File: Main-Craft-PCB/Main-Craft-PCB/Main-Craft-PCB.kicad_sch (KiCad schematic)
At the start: 88 parts, among them J1 Conn_01x10, Q23 BC817, Q25 IRFR9014PBF, Q31 BC817, U10 ZLDO1117G50TA, U2 NUCLEO144-F429ZI, U5 74HC14, U9 ZSR330GTA

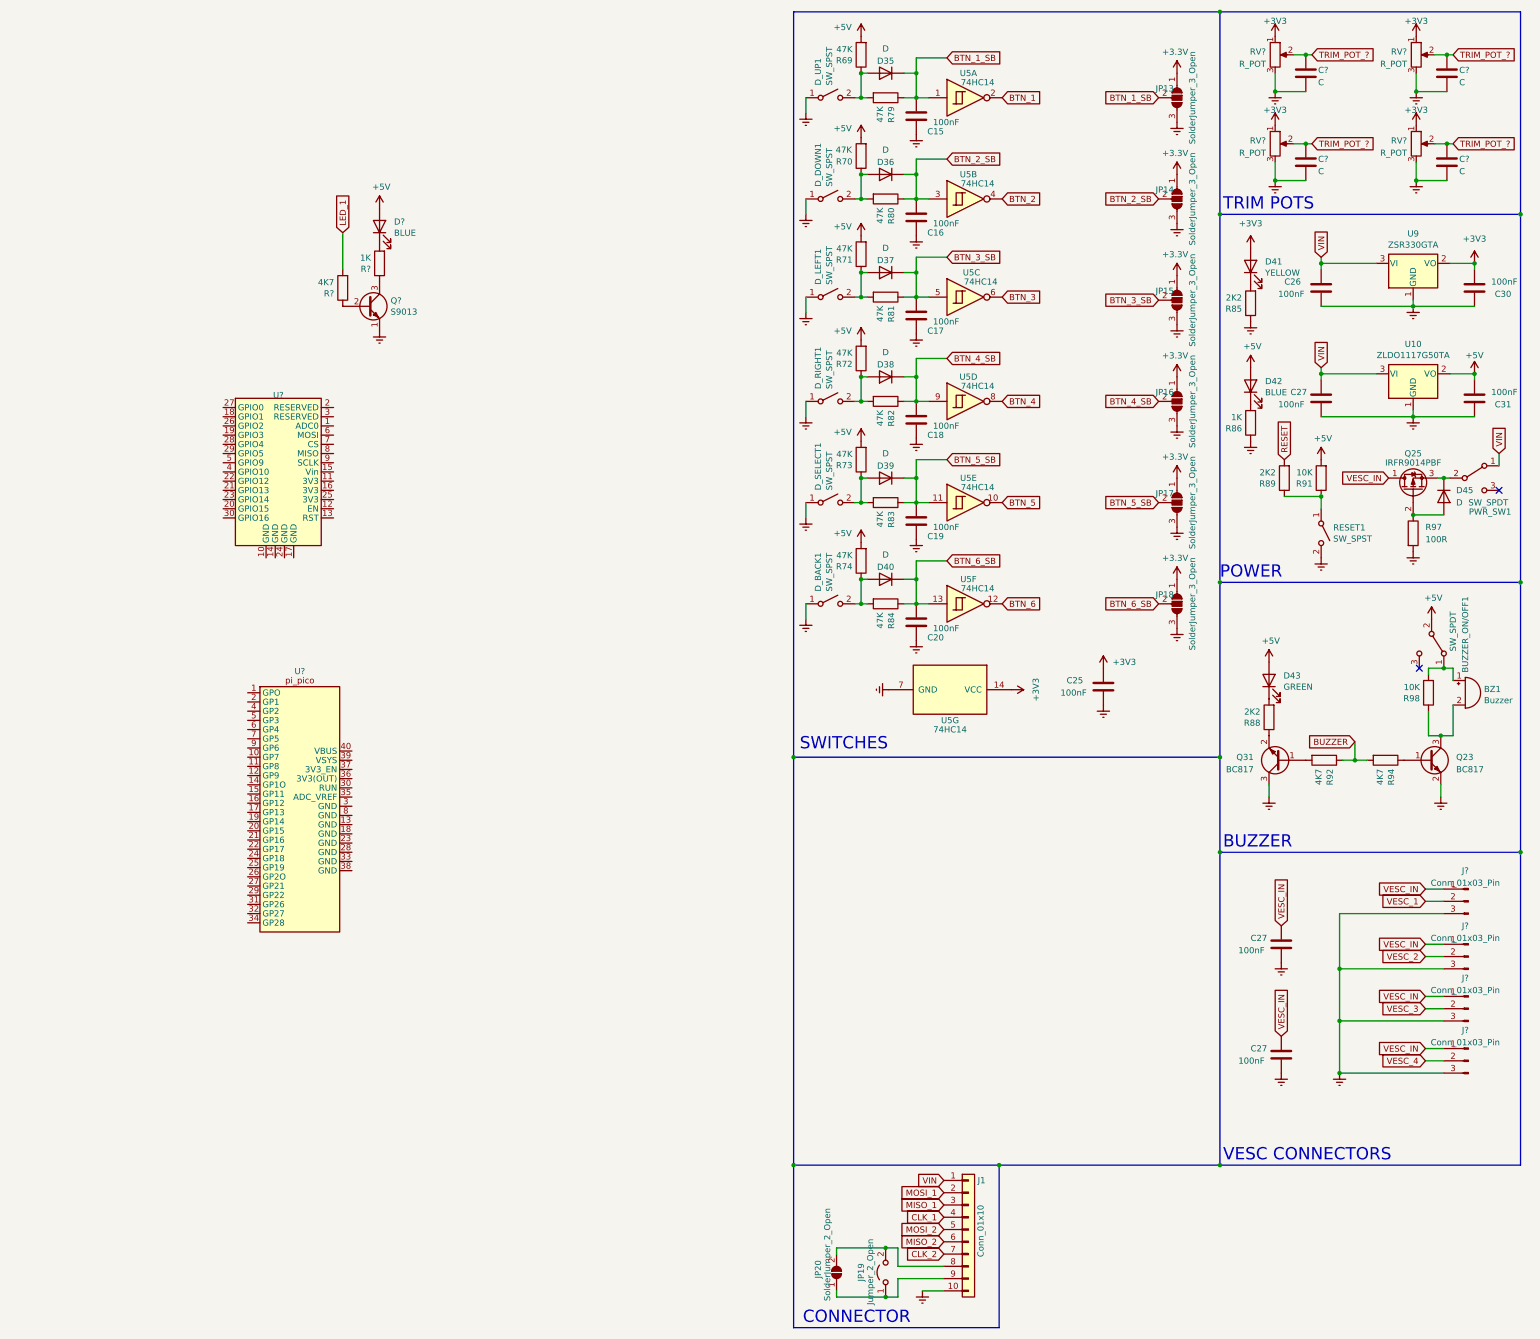
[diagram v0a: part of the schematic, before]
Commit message: Update Schematic, add battery level monitors
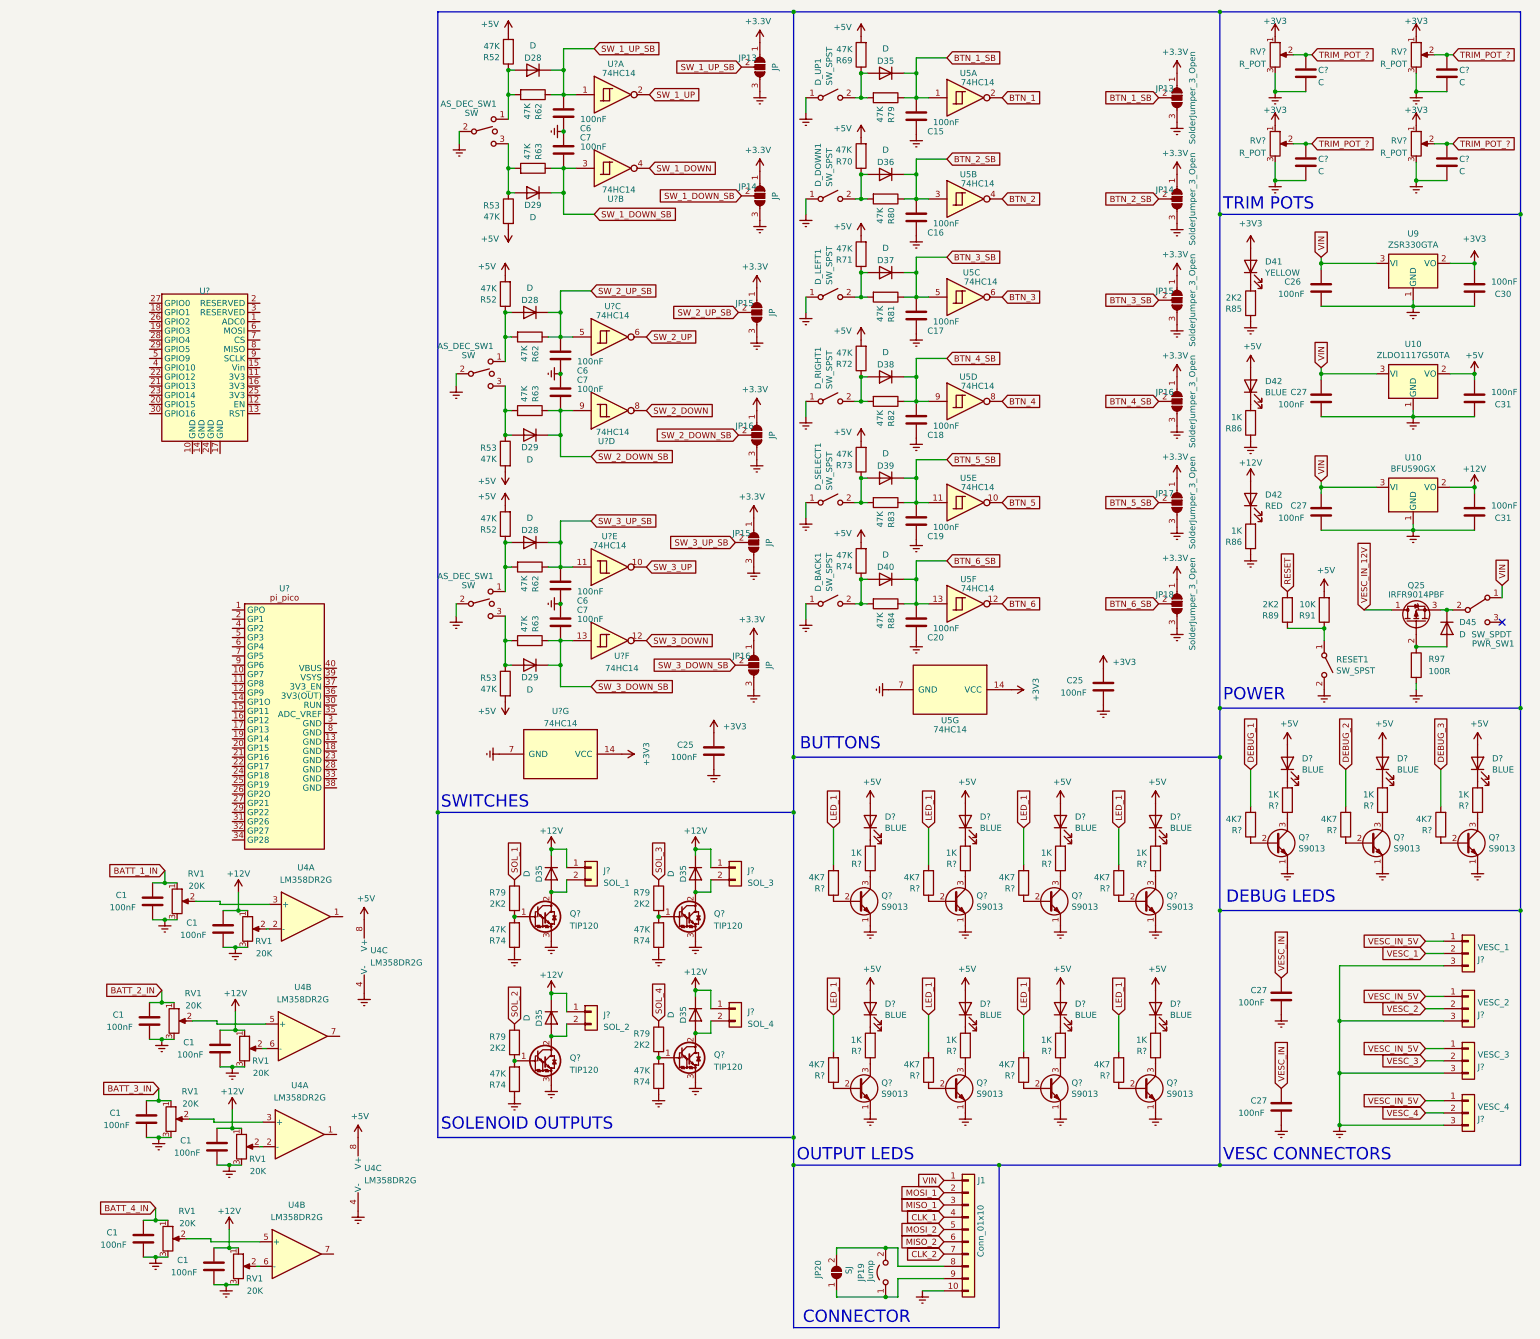
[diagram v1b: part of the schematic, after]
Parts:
- removed BUZZER_ON/OFF1: SW_SPDT, My_library:1Ms1T1B1M1QE, symbol Switch:SW_SPDT
- removed BZ1: Buzzer, My_library:Buzzer, symbol Device:Buzzer
- removed D43: GREEN, LED_SMD:LED_0603_1608Metric, symbol Device:LED
- removed J? (x4): Conn_01x03_Pin, symbol Connector:Conn_01x03_Pin
- removed Q23, Q31: BC817, Package_TO_SOT_SMD:SOT-23, symbol Transistor_BJT:BC817
- removed R88: 2K2, Resistor_SMD:R_0603_1608Metric, symbol Device:R
- removed R92, R94: 4K7, Resistor_SMD:R_0603_1608Metric, symbol Device:R
- removed R98: 10K, Resistor_SMD:R_0603_1608Metric, symbol Device:R
- added AS_DEC_SW1 (x3): SW, My_library:1Ms1T1B1M1QE, symbol Switch:SW_SPDT_MSM
- added C1 (x8), C25, C27, C31, C6 (x3), C7 (x3): 100nF, Capacitor_SMD:C_0603_1608Metric, symbol Device:C
- added D28 (x3), D29 (x3), D35 (x4): D, Diode_SMD:D_SMA, symbol Device:D
- added D42: RED, LED_SMD:LED_0603_1608Metric, symbol Device:LED
- added D? (x10): BLUE, LED_SMD:LED_0603_1608Metric, symbol Device:LED
- added J?: VESC_4, symbol Connector_Generic:Conn_01x03
- added J?: SOL_1, symbol Connector_Generic:Conn_01x02
- added J?: VESC_1, symbol Connector_Generic:Conn_01x03
- added J?: SOL_4, symbol Connector_Generic:Conn_01x02
- added J?: SOL_3, symbol Connector_Generic:Conn_01x02
- added J?: VESC_3, symbol Connector_Generic:Conn_01x03
- added J?: VESC_2, symbol Connector_Generic:Conn_01x03
- added J?: SOL_2, symbol Connector_Generic:Conn_01x02
- added JP13, JP14, JP15 (x2), JP16 (x2): JP, Jumper:SolderJumper-3_P1.3mm_Open_RoundedPad1.0x1.5mm_NumberLabels, symbol Jumper:SolderJumper_3_Open
- added Q? (x10): S9013, Package_TO_SOT_SMD:SOT-23, symbol Transistor_BJT:2N2219
- added Q? (x4): TIP120, Package_TO_SOT_THT:TO-220-3_Vertical, symbol Transistor_BJT:TIP120
- added R52 (x3), R53 (x3), R62 (x3), R63 (x3), R74 (x4): 47K, Resistor_SMD:R_0603_1608Metric, symbol Device:R
- added R79 (x4): 2K2, Resistor_SMD:R_0603_1608Metric, symbol Device:R
- added R86, R? (x10): 1K, Resistor_SMD:R_0603_1608Metric, symbol Device:R
- added R? (x10): 4K7, Resistor_SMD:R_0603_1608Metric, symbol Device:R
- added RV1 (x8): 20K, My_library:Variable_Resistor, symbol Device:R_Potentiometer
- added U10: BFU590GX, Package_TO_SOT_SMD:SOT-223, symbol Regulator_Linear:LM1117-5.0
- added U4 (x2): LM358DR2G, Package_SO:SOP-8_3.76x4.96mm_P1.27mm, symbol Amplifier_Operational:LM358
- added U? (x7): 74HC14, symbol 74xx:74HC14
- JP19: value Jumper_2_Open -> Jump
- JP20: value SolderJumper_2_Open -> SJ
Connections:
- net +3V3: now also C25.1, JP13.1 (A), JP14.1 (A), JP15.1 (A), JP15.1 (A), JP16.1 (A), JP16.1 (A), U?.14 (VCC)
- net +5V: now also D?.2 (A), D?.2 (A), D?.2 (A), D?.2 (A), D?.2 (A), D?.2 (A), D?.2 (A), D?.2 (A), D?.2 (A), D?.2 (A), R52.2, R52.2, R52.2, R53.2, R53.2, R53.2, U4.8 (V+), U4.8 (V+)
- net Earth: now also AS_DEC_SW1.2, AS_DEC_SW1.2, AS_DEC_SW1.2, C1.2, C1.2, C1.2, C1.2, C1.2, C1.2, C1.2, C1.2, C25.2, C27.2, C31.1, C6.1, C6.1, C6.1, C7.1, C7.1, C7.1, J?.3 (Pin_3), J?.3 (Pin_3), J?.3 (Pin_3), J?.3 (Pin_3), JP13.3 (B), JP14.3 (B), JP15.3 (B), JP15.3 (B), JP16.3 (B), JP16.3 (B), Q?.1 (E), Q?.1 (E), Q?.1 (E), Q?.1 (E), Q?.1 (E), Q?.1 (E), Q?.1 (E), Q?.1 (E), Q?.1 (E), Q?.1 (E), Q?.3 (E), Q?.3 (E), Q?.3 (E), Q?.3 (E), R74.1, R74.1, R74.1, R74.1, R86.1, RV1.3, RV1.3, RV1.3, RV1.3, RV1.3, RV1.3, RV1.3, RV1.3, U10.1 (GND), U4.4 (V-), U4.4 (V-), U?.7 (GND)
- net LED_1: now also R?.2, R?.2, R?.2, R?.2, R?.2, R?.2, R?.2
- net VESC_1: now also J?.2 (Pin_2)
- net VESC_2: now also J?.2 (Pin_2)
- net VESC_3: now also J?.2 (Pin_2)
- net VESC_4: now also J?.2 (Pin_2)
- net VESC_IN: no longer Q25.1 (D)
- net VIN: now also C27.1, U10.3 (VI)
- new net: D35.2 (A), J?.2 (Pin_2), Q?.2 (C) (x4)
- new net: Q?.3 (C), R?.1 (x10)
- new net: D?.1 (K), R?.2 (x10)
- new net: AS_DEC_SW1.1, D28.2 (A), R52.1, R62.2 (x3)
- new net: AS_DEC_SW1.3, D29.2 (A), R53.1, R63.2 (x3)
- new net: Q?.2 (B), R?.1 (x10)
- new net: Q?.1 (B), R74.2, R79.2 (x4)
- new net: RV1.2, U4.6 (-) (x2)
- new net: RV1.2, U4.3 (+) (x2)
- new net: D42.1 (K), R86.2
- new net: RV1.2, U4.2 (-) (x2)
- new net: RV1.2, U4.5 (+) (x2)
- new net +12V: C1.1, C1.1, C1.1, C1.1, C31.2, D35.1 (K), D35.1 (K), D35.1 (K), D35.1 (K), D42.2 (A), J?.1 (Pin_1), J?.1 (Pin_1), J?.1 (Pin_1), J?.1 (Pin_1), RV1.1, RV1.1, RV1.1, RV1.1, U10.2 (VO)
- new net BATT_1_IN: C1.1, RV1.1
- new net BATT_2_IN: C1.1, RV1.1
- new net BATT_3_IN: C1.1, RV1.1
- new net BATT_4_IN: C1.1, RV1.1
- new net DEBUG_1: R?.2
- new net DEBUG_2: R?.2
- new net DEBUG_3: R?.2
- new net SOL_1: R79.1
- new net SOL_2: R79.1
- new net SOL_3: R79.1
- new net SOL_4: R79.1
- new net SW_1_DOWN: U?.4
- new net SW_1_DOWN_SB: C7.2, D29.1 (K), JP14.2 (C), R63.1, U?.3
- new net SW_1_UP: U?.2
- new net SW_1_UP_SB: C6.2, D28.1 (K), JP13.2 (C), R62.1, U?.1
- new net SW_2_DOWN: U?.8
- new net SW_2_DOWN_SB: C7.2, D29.1 (K), JP16.2 (C), R63.1, U?.9
- new net SW_2_UP: U?.6
- new net SW_2_UP_SB: C6.2, D28.1 (K), JP15.2 (C), R62.1, U?.5
- new net SW_3_DOWN: U?.12
- new net SW_3_DOWN_SB: C7.2, D29.1 (K), JP16.2 (C), R63.1, U?.13
- new net SW_3_UP: U?.10
- new net SW_3_UP_SB: C6.2, D28.1 (K), JP15.2 (C), R62.1, U?.11
- new net VESC_IN_12V: Q25.1 (D)
- new net VESC_IN_5V: J?.1 (Pin_1), J?.1 (Pin_1), J?.1 (Pin_1), J?.1 (Pin_1)
- no-connect marks 2 -> 1
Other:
- note added: "BUTTONS"
- note added: "DEBUG LEDS"
- note added: "OUTPUT LEDS"
- note added: "SOLENOID OUTPUTS"
- note removed: "BUZZER"
- moved on the sheet: C27, D45, D?, PWR_SW1, Q25, Q?, R89, R91, R97, R?, RESET1, U?

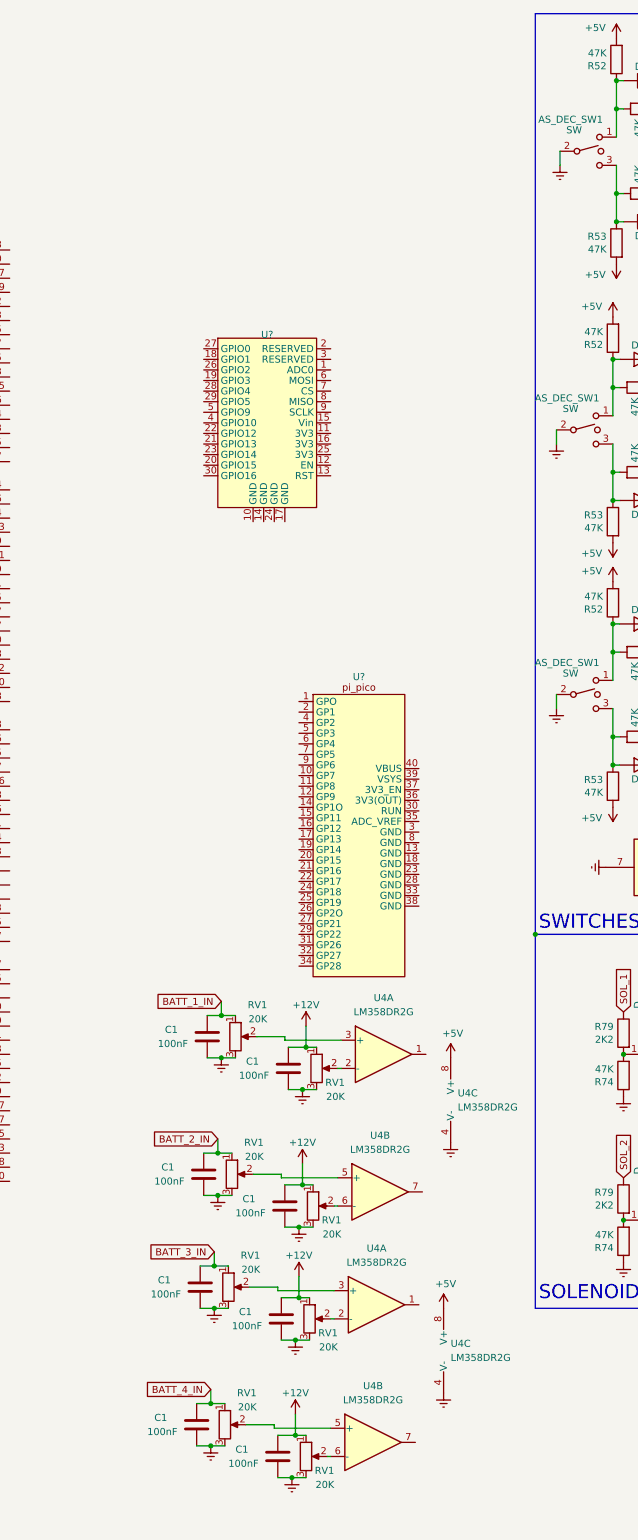
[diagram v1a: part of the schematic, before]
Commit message: Add UART MUX
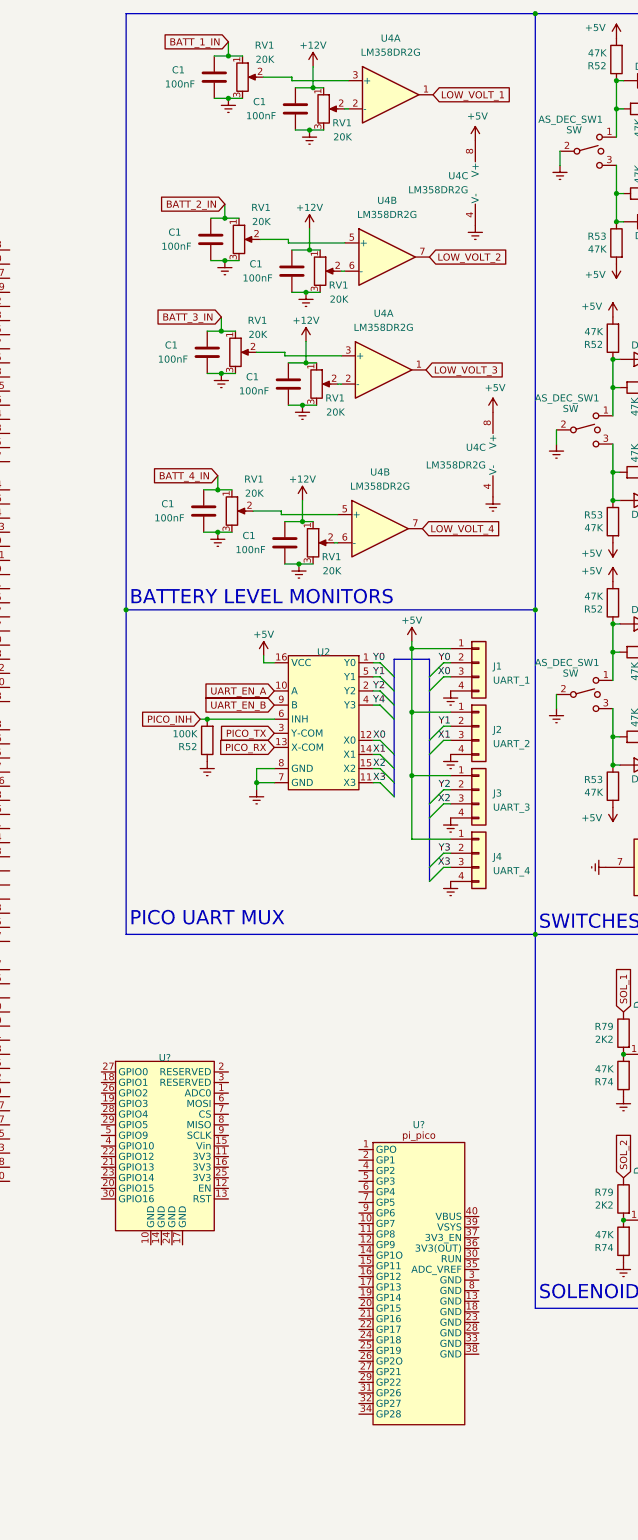
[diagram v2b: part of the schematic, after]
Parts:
- added J1: UART_1, symbol Connector_Generic:Conn_01x04
- added J2: UART_2, symbol Connector_Generic:Conn_01x04
- added J3: UART_3, symbol Connector_Generic:Conn_01x04
- added J4: UART_4, symbol Connector_Generic:Conn_01x04
- added R52: 100K, Resistor_SMD:R_0603_1608Metric, symbol Device:R
- added U2: ~, symbol My_Library.lib:SN74LV4052A
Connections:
- net +5V: now also J1.1 (Pin_1), J2.1 (Pin_1), J3.1 (Pin_1), J4.1 (Pin_1), U2.16 (VCC)
- net Earth: now also J1.4 (Pin_4), J2.4 (Pin_4), J3.4 (Pin_4), J4.4 (Pin_4), R52.1, U2.7 (GND), U2.8 (GND)
- net LOW_VOLT_3: now reaches U4.1
- net LOW_VOLT_1: now reaches U4.1
- net LOW_VOLT_4: now reaches U4.7
- net LOW_VOLT_2: now reaches U4.7
- new net PICO_INH: R52.2, U2.6 (INH)
- new net PICO_RX: U2.13 (X-COM)
- new net PICO_TX: U2.3 (Y-COM)
- new net UART_EN_A: U2.10 (A)
- new net UART_EN_B: U2.9 (B)
- new net X0: J1.3 (Pin_3), U2.12 (X0)
- new net X1: J2.3 (Pin_3), U2.14 (X1)
- new net X2: J3.3 (Pin_3), U2.15 (X2)
- new net X3: J4.3 (Pin_3), U2.11 (X3)
- new net Y0: J1.2 (Pin_2), U2.1 (Y0)
- new net Y1: J2.2 (Pin_2), U2.5 (Y1)
- new net Y2: J3.2 (Pin_2), U2.2 (Y2)
- new net Y3: J4.2 (Pin_2)
- new net Y4: U2.4 (Y3)
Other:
- note added: "BATTERY LEVEL MONITORS"
- note added: "PICO UART MUX"
- moved on the sheet: C1, RV1, U4A, U4B, U4C, U?

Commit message: add all required interfaces to PCB - just need to label up
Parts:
- removed JP19: Jump, My_library:Jumper, symbol Jumper:Jumper_2_Open
- removed JP20: SJ, Jumper:SolderJumper-2_P1.3mm_Open_RoundedPad1.0x1.5mm, symbol Jumper:SolderJumper_2_Open
- added C1: 470uF, symbol Device:C_Polarized
- added C27: 100nF, Capacitor_SMD:C_0603_1608Metric, symbol Device:C
- added J11: PWR_IN, symbol Connector_Generic:Conn_01x02
- added J19: S500_1, symbol Connector_Generic:Conn_01x03
- added J20: S500_2, symbol Connector_Generic:Conn_01x03
- added J21: S500_3, symbol Connector_Generic:Conn_01x03
- added J22: S500_4, symbol Connector_Generic:Conn_01x03
- added J23, J24, J25, J26: LEDS, symbol Connector_Generic:Conn_01x02
- added J5: RELAY_1, symbol Connector_Generic:Conn_01x03
- added J6: RELAY_2, symbol Connector_Generic:Conn_01x03
- added J7, J8: RELAY_3, symbol Connector_Generic:Conn_01x03
- added R2: 47K, Resistor_SMD:R_0603_1608Metric, symbol Device:R
- added R3, R4: 1K, Resistor_SMD:R_0603_1608Metric, symbol Device:R
- added U5: LM358, symbol Amplifier_Operational:LM358
- U3: renamed from U?; value ~ -> ESP8266
- U4: renamed from U2; value ~ -> SN74LV4052
- U8: renamed from U?; value ~ -> Pi Pico
- gave numbers to parts that had none: 65
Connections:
- net +12V: now also J1.8 (Pin_8), J23.1 (Pin_1), J24.1 (Pin_1), J25.1 (Pin_1), J26.1 (Pin_1), R3.2
- net +3V3: now also U8.39 (VSYS)
- net +5V: now also U3.15 (Vin), J19.2 (Pin_2), J20.2 (Pin_2), J21.2 (Pin_2), J22.2 (Pin_2), J5.2 (Pin_2), J6.2 (Pin_2), J7.2 (Pin_2), J8.2 (Pin_2), U5.8 (V+)
- net Earth: now also U2.104 (AGND), U2.111 (GND), U2.126 (GND), U2.135 (GND), U2.143 (GND), U2.144 (GND), U2.19 (GND), U2.20 (GND), U2.22 (GND), U2.49 (GND), U2.60 (GND), U2.71 (GND), U2.72 (GND), U2.8 (GND), U2.81 (GND), U2.92 (GND), U3.10 (GND), U3.14 (GND), U3.17 (GND), U3.24 (GND), U8.13 (GND), U8.18 (GND), U8.23 (GND), U8.28 (GND), U8.3 (GND), U8.33 (GND), U8.38 (GND), U8.8 (GND), C1.2, C27.2, J11.2 (Pin_2), J19.3 (Pin_3), J20.3 (Pin_3), J21.3 (Pin_3), J22.3 (Pin_3), J23.2 (Pin_2), J24.2 (Pin_2), J25.2 (Pin_2), J26.2 (Pin_2), J5.3 (Pin_3), J6.3 (Pin_3), J7.3 (Pin_3), J8.3 (Pin_3), R2.2, R4.1, U5.4 (V-)
- net PICO_INH: now also U8.4 (GP2)
- net PICO_RX: now also U8.2 (GP1)
- net PICO_TX: now also U8.1 (GPO)
- net UART_EN_A: now also U8.5 (GP3)
- net UART_EN_B: now also U8.6 (GP4)
- net VIN: now also C1.1
- net I2C_ESP_SDA: now reaches U3.28 (GPIO4)
- net I2C_ESP_SCl: now reaches U3.29 (GPIO5)
- net I2C_PICO_SDA: now reaches U8.11 (GP8)
- net I2C_PICO_SCl: now reaches U8.12 (GP9)
- net CON_CONNECTION: now reaches J1.9 (Pin_9)
- net CON_CONNECTION: now also R2.1, U5.3 (+)
- net VESC_IN_12V renamed 12V_INPUT
- net 12V_INPUT: now also C27.1, J11.1 (Pin_1)
- new net: R3.1, R4.2, U5.2 (-)
- new net CON_INPUT: U5.1
- new net RELAY_1: J5.1 (Pin_1)
- new net RELAY_2: J6.1 (Pin_1)
- new net RELAY_3: J7.1 (Pin_1)
- new net RELAY_4: J8.1 (Pin_1)
- new net S500_1: J19.1 (Pin_1)
- new net S500_2: J20.1 (Pin_1)
- new net S500_3: J21.1 (Pin_1)
- new net S500_4: J22.1 (Pin_1)
- no-connect marks 1 -> 51
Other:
- note added: "CONNECTION COMPARATOR"
- note added: "LEDS"
- note added: "POWER IN"
- note added: "RELAYS"
- note added: "SERVOS"
- moved on the sheet: D45, PWR_SW1, Q25, R89, R91, R97, RESET1, U2, U3
